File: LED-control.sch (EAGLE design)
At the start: 31 parts

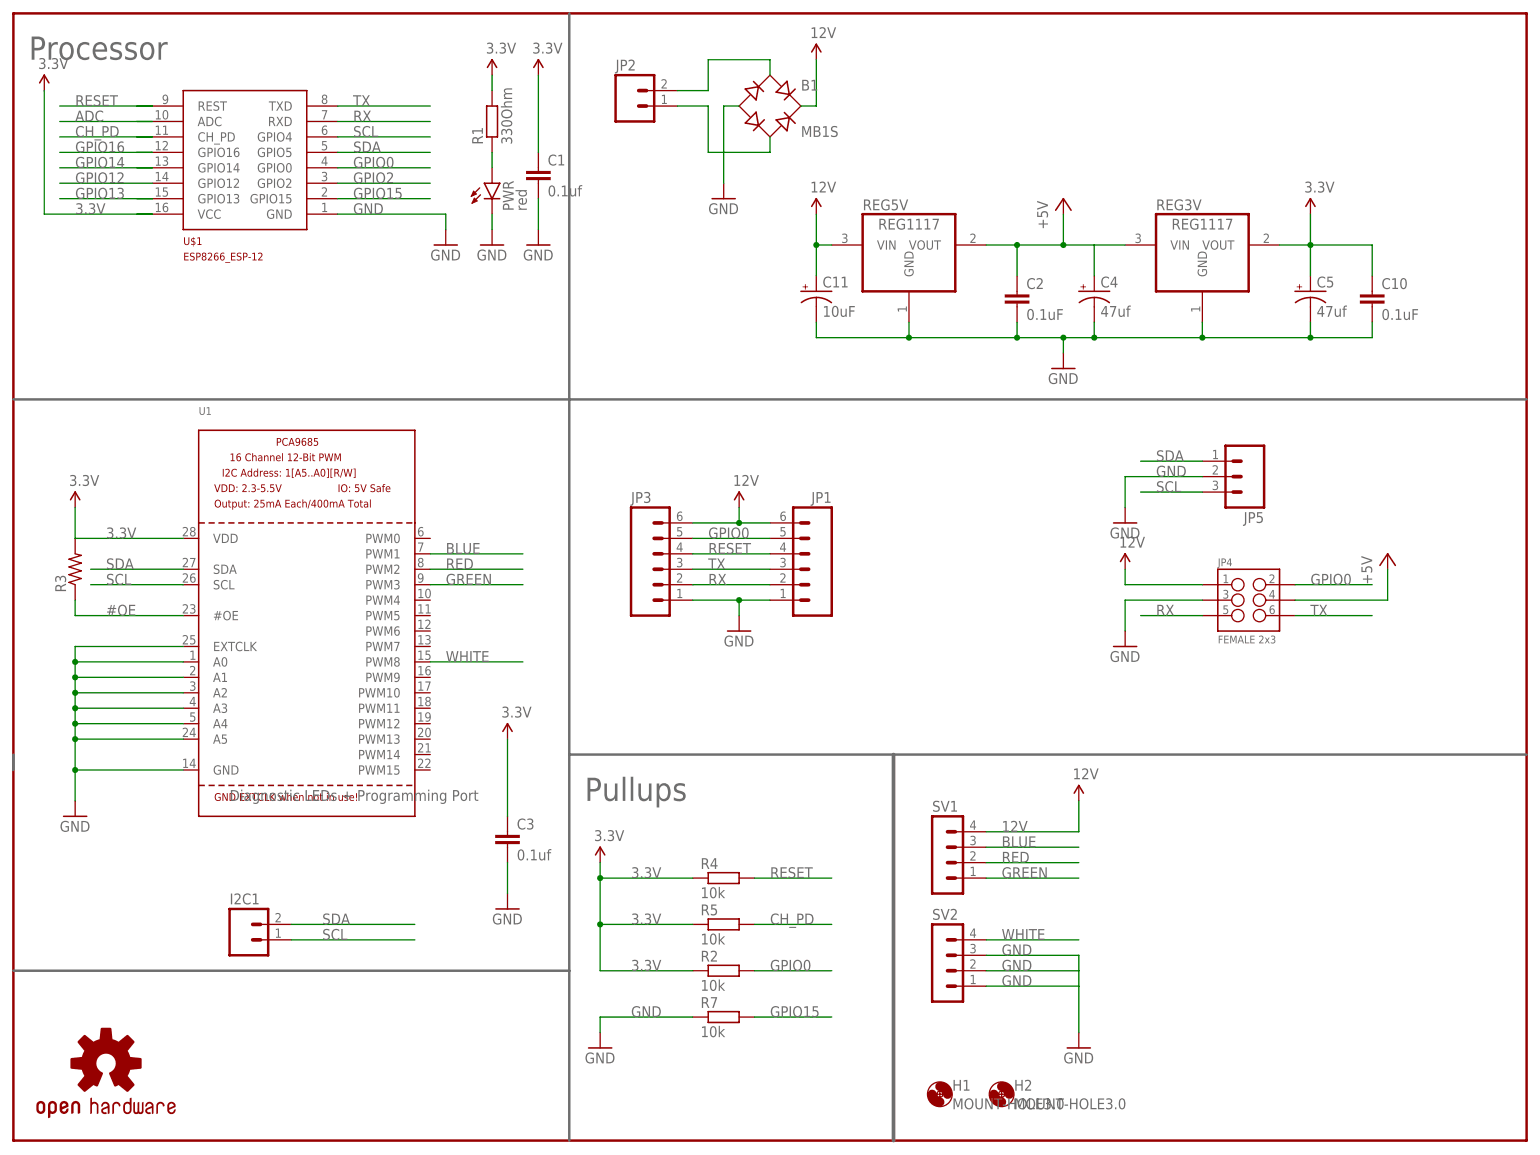
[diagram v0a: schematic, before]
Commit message: Reworking board to standardise on 1206 caps and resistors. Moving caps into the center where they'll clip through the hole in the top board. Move power connector to rear (duh). Remove i2c connectors. Replace programming harness connector with better one, with i2c. Add i2c pullups.
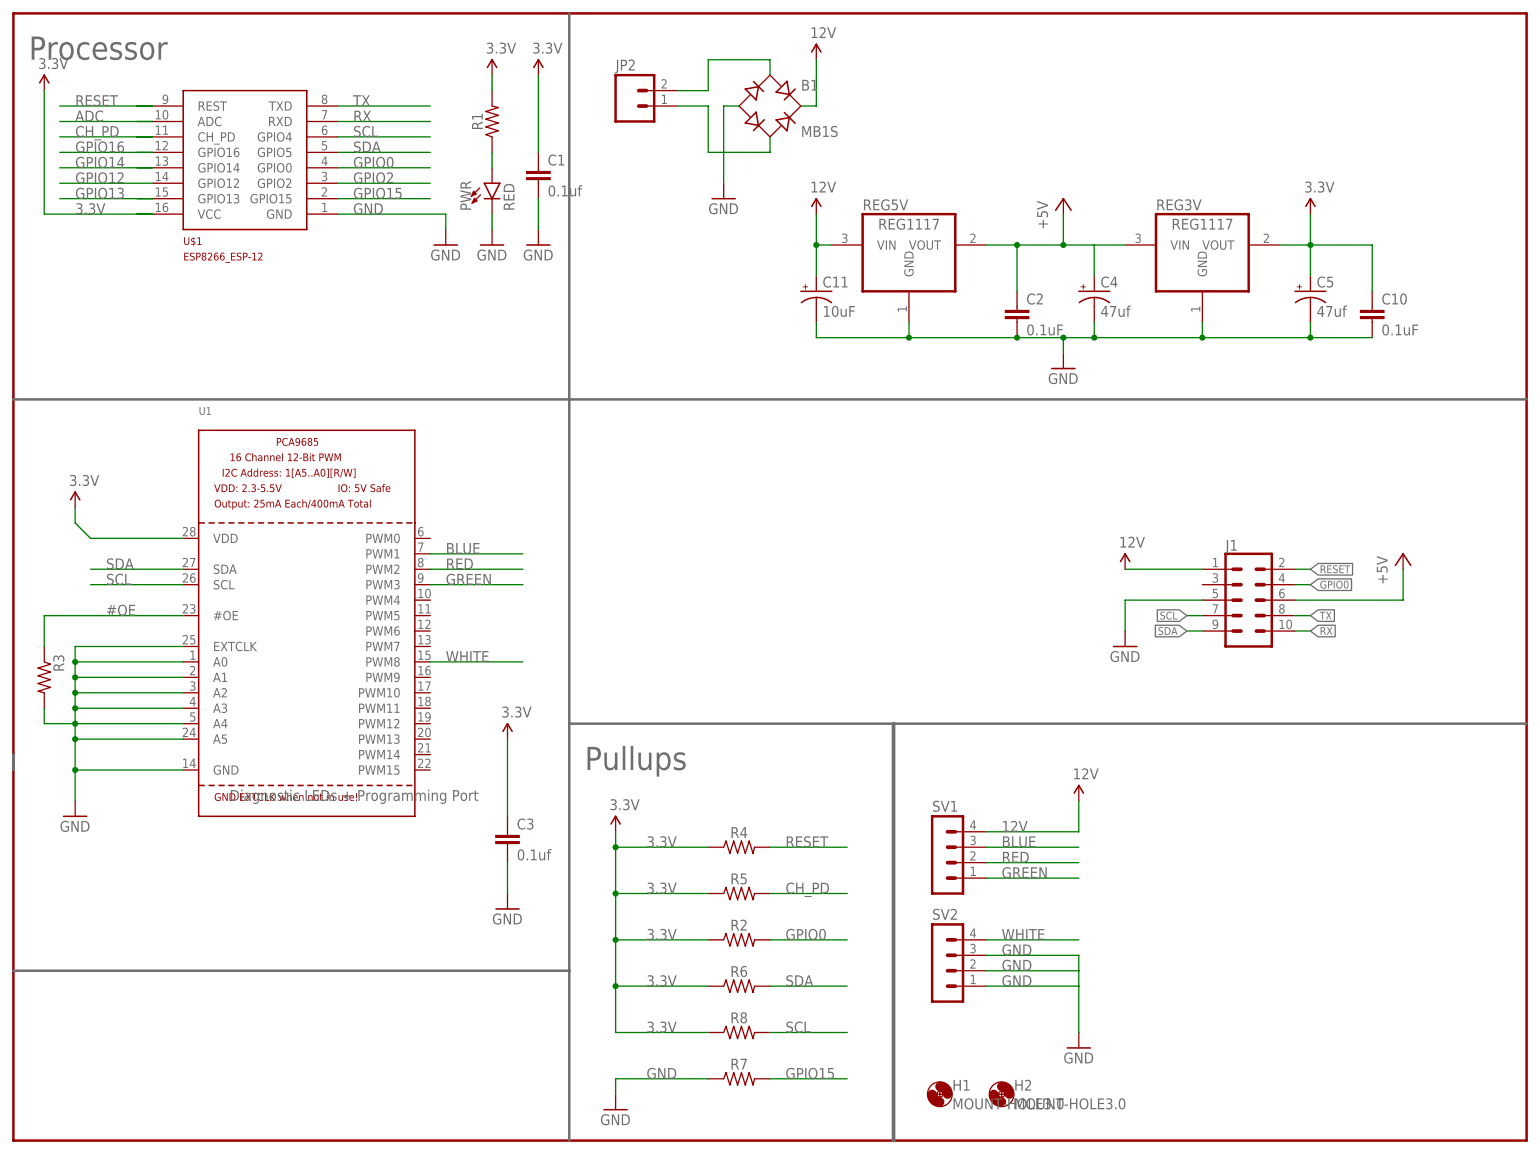
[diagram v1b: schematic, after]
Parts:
- removed I2C1: (no value), SparkFun-Connectors:M02-JST-2-PTH-NO_SILK
- removed JP1: (no value), SparkFun-Connectors:M06SMD-STRAIGHT-COMBO-FEMALE
- removed JP3: (no value), SparkFun-Connectors:M061X06-SMD_EDGE_FEMALE
- removed JP4: FEMALE 2x3, SparkFun-Connectors:M03X2FEMALE
- removed JP5: (no value), SparkFun-Connectors:M03PTH
- removed LOGO2: OSHW-LOGOS, SparkFun-Aesthetics:OSHW-LOGOS
- added J1: (no value), SparkFun-Connectors:CONN_05X2SHD
- added R6, R8: (no value), SparkFun-Resistors:RESISTOR1206
- C1, C3: device rcl:C-EUC0805 -> rcl:C-EUC1206
- C10, C2: device SparkFun-Capacitors:0.1UF-25V(+80/-20%)(0603) -> rcl:C-EUC1206
- PWR: value red -> RED; device SparkFun-LED:LED0603 -> SparkFun-LED:LED-RED1206
- R1: value 330Ohm -> (none); device rcl:R-EU_R0805 -> SparkFun-Resistors:RESISTOR1206
- R2, R4, R5, R7: value 10k -> (none); device rcl:R-EU_R0805 -> SparkFun-Resistors:RESISTOR1206
- R3: value (none) -> (none); device SparkFun-Resistors:RESISTOR0603 -> rcl:R-US_R1206
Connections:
- net +5V: now also J1.6; no longer JP4.4
- net 12V: now also J1.1; no longer JP1.6, JP3.6, JP4.1
- net 3.3V: now also R6.1, R8.1; no longer R3.2
- net GND: now also J1.5, R3.2; no longer JP1.1, JP3.1, JP4.3, JP5.2
- net GPIO0: now also J1.4; no longer JP1.5, JP3.5, JP4.2
- net RESET: now also J1.2; no longer JP1.4, JP3.4
- net RX: now also J1.10; no longer JP1.2, JP3.2, JP4.5
- net SCL: now also J1.7, R8.2; no longer I2C1.1, JP5.3
- net SDA: now also J1.9, R6.2; no longer I2C1.2, JP5.1
- net TX: now also J1.8; no longer JP1.3, JP3.3, JP4.6
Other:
- moved on the sheet: C10, C2, R3

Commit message: Finalised board design
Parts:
- removed J1: (no value), SparkFun-Connectors:CONN_05X2SHD
- added J2: (no value), SparkFun-Connectors:CONN_05X2SHD
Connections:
- net +5V: now also J2.7; no longer J1.6
- net 12V: now also J2.9; no longer J1.1
- net 3.3V: now also J2.5
- net GND: now also J2.6; no longer J1.5
- net GPIO0: now also J2.8; no longer J1.4
- net RESET: now also J2.10; no longer J1.2
- net RX: now also J2.4; no longer J1.10
- net SCL: now also J2.1; no longer J1.7
- net SDA: now also J2.3; no longer J1.9
- net TX: now also J2.2; no longer J1.8
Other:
- moved on the sheet: H1, H2
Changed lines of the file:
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@@
 <part name="SUPPLY1" library="SparkFun-Aesthetics" deviceset="3.3V" device=""/>
 <part name="SUPPLY3" library="SparkFun-Aesthetics" deviceset="3.3V" device=""/>
-<part name="SUPPLY13" library="SparkFun-Aesthetics" deviceset="12V" device=""/>
-<part name="P+2" library="supply1" deviceset="+5V" device=""/>
-<part name="GND11" library="supply1" deviceset="GND" device=""/>
 <part name="R6" library="SparkFun-Resistors" deviceset="RESISTOR" device="1206" value=" "/>
 <part name="R8" library="SparkFun-Resistors" deviceset="RESISTOR" device="1206" value=" "/>
-<part name="J1" library="SparkFun-Connectors" deviceset="CONN_05X2" device="SHD"/>
+<part name="J2" library="SparkFun-Connectors" deviceset="CONN_05X2" device="SHD"/>
 </parts>
 <sheets>
@@
 <instance part="SV2" gate="1" x="152.4" y="30.48"/>
 <instance part="SUPPLY2" gate="G$1" x="175.26" y="55.88"/>
-<instance part="H1" gate="G$1" x="152.4" y="7.62"/>
-<instance part="H2" gate="G$1" x="162.56" y="7.62"/>
+<instance part="H1" gate="G$1" x="218.44" y="58.42"/>
+<instance part="H2" gate="G$1" x="218.44" y="50.8"/>
 <instance part="GND3" gate="1" x="175.26" y="15.24"/>
 <instance part="U$1" gate="G$1" x="45.72" y="162.56"/>
@@
 <instance part="SUPPLY1" gate="G$1" x="81.28" y="66.04"/>
 <instance part="SUPPLY3" gate="G$1" x="213.36" y="152.4"/>
-<instance part="SUPPLY13" gate="G$1" x="182.88" y="93.98"/>
-<instance part="P+2" gate="1" x="228.6" y="96.52"/>
-<instance part="GND11" gate="1" x="182.88" y="81.28"/>
 <instance part="R6" gate="G$1" x="119.38" y="25.4"/>
 <instance part="R8" gate="G$1" x="119.38" y="17.78"/>
-<instance part="J1" gate="G$1" x="203.2" y="88.9"/>
+<instance part="J2" gate="G$1" x="205.74" y="91.44"/>
 </instances>
 <busses>
@@
 </segment>
 <segment>
-<pinref part="J1" gate="G$1" pin="10"/>
-<wire x1="210.82" y1="83.82" x2="213.36" y2="83.82" width="0.1524" layer="91"/>
-<label x="213.36" y="83.82" size="1.27" layer="95" xref="yes"/>
+<wire x1="213.36" y1="93.98" x2="215.9" y2="93.98" width="0.1524" layer="91"/>
+<label x="215.9" y="93.98" size="1.27" layer="95" xref="yes"/>
+<pinref part="J2" gate="G$1" pin="4"/>
 </segment>
 </net>
@@
 </segment>
 <segment>
-<pinref part="J1" gate="G$1" pin="2"/>
-<wire x1="210.82" y1="93.98" x2="213.36" y2="93.98" width="0.1524" layer="91"/>
-<label x="213.36" y="93.98" size="1.27" layer="95" xref="yes"/>
+<wire x1="213.36" y1="86.36" x2="215.9" y2="86.36" width="0.1524" layer="91"/>
+<label x="215.9" y="86.36" size="1.27" layer="95" xref="yes"/>
+<pinref part="J2" gate="G$1" pin="10"/>
 </segment>
 </net>
@@
 <pinref part="SUPPLY6" gate="G$1" pin="3.3V"/>
 <wire x1="10.16" y1="101.6" x2="10.16" y2="104.14" width="0.1524" layer="91"/>
+</segment>
+<segment>
+<wire x1="198.12" y1="91.44" x2="195.58" y2="91.44" width="0.1524" layer="91"/>
+<label x="195.58" y="91.44" size="1.27" layer="95" rot="R180" xref="yes"/>
+<pinref part="J2" gate="G$1" pin="5"/>
 </segment>
 </net>
@@
 </segment>
 <segment>
-<wire x1="195.58" y1="88.9" x2="182.88" y2="88.9" width="0.1524" layer="91"/>
-<wire x1="182.88" y1="88.9" x2="182.88" y2="83.82" width="0.1524" layer="91"/>
-<pinref part="GND11" gate="1" pin="GND"/>
-<pinref part="J1" gate="G$1" pin="5"/>
+<wire x1="213.36" y1="91.44" x2="215.9" y2="91.44" width="0.1524" layer="91"/>
+<label x="215.9" y="91.44" size="1.27" layer="95" xref="yes"/>
+<pinref part="J2" gate="G$1" pin="6"/>
 </segment>
 </net>
@@
 </segment>
 <segment>
-<pinref part="J1" gate="G$1" pin="9"/>
-<wire x1="193.04" y1="83.82" x2="195.58" y2="83.82" width="0.1524" layer="91"/>
-<label x="193.04" y="83.82" size="1.27" layer="95" rot="R180" xref="yes"/>
+<wire x1="198.12" y1="93.98" x2="195.58" y2="93.98" width="0.1524" layer="91"/>
+<label x="195.58" y="93.98" size="1.27" layer="95" rot="R180" xref="yes"/>
+<pinref part="J2" gate="G$1" pin="3"/>
 </segment>
 </net>
@@
 </segment>
 <segment>
-<wire x1="210.82" y1="86.36" x2="213.36" y2="86.36" width="0.1524" layer="91"/>
-<pinref part="J1" gate="G$1" pin="8"/>
-<label x="213.36" y="86.36" size="1.27" layer="95" xref="yes"/>
+<wire x1="213.36" y1="96.52" x2="215.9" y2="96.52" width="0.1524" layer="91"/>
+<label x="215.9" y="96.52" size="1.27" layer="95" xref="yes"/>
+<pinref part="J2" gate="G$1" pin="2"/>
 </segment>
 </net>
@@
 </segment>
 <segment>
-<pinref part="J1" gate="G$1" pin="7"/>
-<wire x1="195.58" y1="86.36" x2="193.04" y2="86.36" width="0.1524" layer="91"/>
-<label x="193.04" y="86.36" size="1.27" layer="95" rot="R180" xref="yes"/>
+<wire x1="195.58" y1="96.52" x2="198.12" y2="96.52" width="0.1524" layer="91"/>
+<label x="195.58" y="96.52" size="1.27" layer="95" rot="R180" xref="yes"/>
+<pinref part="J2" gate="G$1" pin="1"/>
 </segment>
 </net>
@@
 </segment>
 <segment>
-<wire x1="210.82" y1="91.44" x2="213.36" y2="91.44" width="0.1524" layer="91"/>
-<pinref part="J1" gate="G$1" pin="4"/>
-<label x="213.36" y="91.44" size="1.27" layer="95" xref="yes"/>
+<wire x1="213.36" y1="88.9" x2="215.9" y2="88.9" width="0.1524" layer="91"/>
+<label x="215.9" y="88.9" size="1.27" layer="95" xref="yes"/>
+<pinref part="J2" gate="G$1" pin="8"/>
 </segment>
 </net>
@@
 </segment>
 <segment>
-<wire x1="195.58" y1="93.98" x2="182.88" y2="93.98" width="0.1524" layer="91"/>
-<pinref part="SUPPLY13" gate="G$1" pin="12V"/>
-<pinref part="J1" gate="G$1" pin="1"/>
+<wire x1="198.12" y1="86.36" x2="195.58" y2="86.36" width="0.1524" layer="91"/>
+<label x="195.58" y="86.36" size="1.27" layer="95" rot="R180" xref="yes"/>
+<pinref part="J2" gate="G$1" pin="9"/>
 </segment>
 </net>
@@
 </segment>
 <segment>
-<wire x1="210.82" y1="88.9" x2="228.6" y2="88.9" width="0.1524" layer="91"/>
-<wire x1="228.6" y1="88.9" x2="228.6" y2="93.98" width="0.1524" layer="91"/>
-<pinref part="P+2" gate="1" pin="+5V"/>
-<pinref part="J1" gate="G$1" pin="6"/>
-</segment>
-</net>
+<wire x1="198.12" y1="88.9" x2="195.58" y2="88.9" width="0.1524" layer="91"/>
+<label x="195.58" y="88.9" size="1.27" layer="95" rot="R180" xref="yes"/>
+<pinref part="J2" gate="G$1" pin="7"/>
+</segment>
+</net>

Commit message: mk10
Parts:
- added R9: 470, SparkFun-Resistors:RESISTOR1206
- R2, R4, R5, R6, R7, R8: value (none) -> 10k
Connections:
- net GPIO16: now also R9.1
- net RESET: now also R9.2
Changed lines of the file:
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@@
 <part name="SUPPLY10" library="SparkFun-Aesthetics" deviceset="3.3V" device=""/>
 <part name="R1" library="SparkFun-Resistors" deviceset="RESISTOR" device="1206" value=" "/>
-<part name="R4" library="SparkFun-Resistors" deviceset="RESISTOR" device="1206" value=" "/>
-<part name="R5" library="SparkFun-Resistors" deviceset="RESISTOR" device="1206" value=" "/>
-<part name="R2" library="SparkFun-Resistors" deviceset="RESISTOR" device="1206" value=" "/>
-<part name="R7" library="SparkFun-Resistors" deviceset="RESISTOR" device="1206" value=" "/>
+<part name="R4" library="SparkFun-Resistors" deviceset="RESISTOR" device="1206" value="10k"/>
+<part name="R5" library="SparkFun-Resistors" deviceset="RESISTOR" device="1206" value="10k"/>
+<part name="R2" library="SparkFun-Resistors" deviceset="RESISTOR" device="1206" value="10k"/>
+<part name="R7" library="SparkFun-Resistors" deviceset="RESISTOR" device="1206" value="10k"/>
 <part name="FRAME1" library="SparkFun-Aesthetics" deviceset="FRAME-LETTER" device="NO_PACKAGE"/>
 <part name="PWR" library="SparkFun-LED" deviceset="LED-RED" device="1206" value="RED"/>
@@
 <part name="SUPPLY1" library="SparkFun-Aesthetics" deviceset="3.3V" device=""/>
 <part name="SUPPLY3" library="SparkFun-Aesthetics" deviceset="3.3V" device=""/>
-<part name="R6" library="SparkFun-Resistors" deviceset="RESISTOR" device="1206" value=" "/>
-<part name="R8" library="SparkFun-Resistors" deviceset="RESISTOR" device="1206" value=" "/>
+<part name="R6" library="SparkFun-Resistors" deviceset="RESISTOR" device="1206" value="10k"/>
+<part name="R8" library="SparkFun-Resistors" deviceset="RESISTOR" device="1206" value="10k"/>
 <part name="J2" library="SparkFun-Connectors" deviceset="CONN_05X2" device="SHD"/>
+<part name="R9" library="SparkFun-Resistors" deviceset="RESISTOR" device="1206" value="470"/>
 </parts>
 <sheets>
@@
 <wire x1="0" y1="121.92" x2="91.44" y2="121.92" width="0.4064" layer="95"/>
 <wire x1="91.44" y1="121.92" x2="91.44" y2="185.42" width="0.4064" layer="95"/>
-<wire x1="91.44" y1="121.92" x2="91.44" y2="68.58" width="0.4064" layer="95"/>
+<wire x1="91.44" y1="121.92" x2="91.44" y2="78.74" width="0.4064" layer="95"/>
 <wire x1="0" y1="63.5" x2="0" y2="60.96" width="0.4064" layer="95"/>
-<wire x1="91.44" y1="68.58" x2="91.44" y2="27.94" width="0.4064" layer="95"/>
+<wire x1="91.44" y1="78.74" x2="91.44" y2="27.94" width="0.4064" layer="95"/>
 <wire x1="91.44" y1="27.94" x2="0" y2="27.94" width="0.4064" layer="95"/>
-<wire x1="91.44" y1="68.58" x2="144.78" y2="68.58" width="0.4064" layer="95"/>
-<wire x1="144.78" y1="68.58" x2="248.92" y2="68.58" width="0.4064" layer="95"/>
+<wire x1="91.44" y1="78.74" x2="144.78" y2="78.74" width="0.4064" layer="95"/>
+<wire x1="144.78" y1="78.74" x2="246.38" y2="78.74" width="0.4064" layer="95"/>
 <wire x1="91.44" y1="121.92" x2="248.92" y2="121.92" width="0.4064" layer="95"/>
 <text x="2.54" y="177.8" size="3.81" layer="95">Processor</text>
-<text x="93.98" y="60.96" size="3.81" layer="95">Pullups</text>
+<text x="93.98" y="71.12" size="3.81" layer="95">Pullups</text>
 <wire x1="91.44" y1="27.94" x2="91.44" y2="0" width="0.4064" layer="95"/>
-<wire x1="144.78" y1="68.58" x2="144.78" y2="0" width="0.6096" layer="95"/>
+<wire x1="144.78" y1="78.74" x2="144.78" y2="0" width="0.6096" layer="95"/>
 <text x="35.56" y="55.88" size="1.778" layer="95">Diagnostic LEDs + Programming Port</text>
 </plain>
@@
 <instance part="R8" gate="G$1" x="119.38" y="17.78"/>
 <instance part="J2" gate="G$1" x="205.74" y="91.44"/>
+<instance part="R9" gate="G$1" x="119.38" y="60.96"/>
 </instances>
 <busses>
@@
 <pinref part="J2" gate="G$1" pin="10"/>
 </segment>
+<segment>
+<pinref part="R9" gate="G$1" pin="2"/>
+<wire x1="124.46" y1="60.96" x2="137.16" y2="60.96" width="0.1524" layer="91"/>
+<label x="127" y="60.96" size="1.778" layer="95"/>
+</segment>
 </net>
 <net name="ADC" class="0">
@@
 <wire x1="22.86" y1="162.56" x2="20.32" y2="162.56" width="0.1524" layer="91"/>
 </segment>
+<segment>
+<pinref part="R9" gate="G$1" pin="1"/>
+<wire x1="99.06" y1="60.96" x2="114.3" y2="60.96" width="0.1524" layer="91"/>
+<label x="104.14" y="60.96" size="1.778" layer="95"/>
+</segment>
 </net>
